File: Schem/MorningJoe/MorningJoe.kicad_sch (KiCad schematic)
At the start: 0 parts

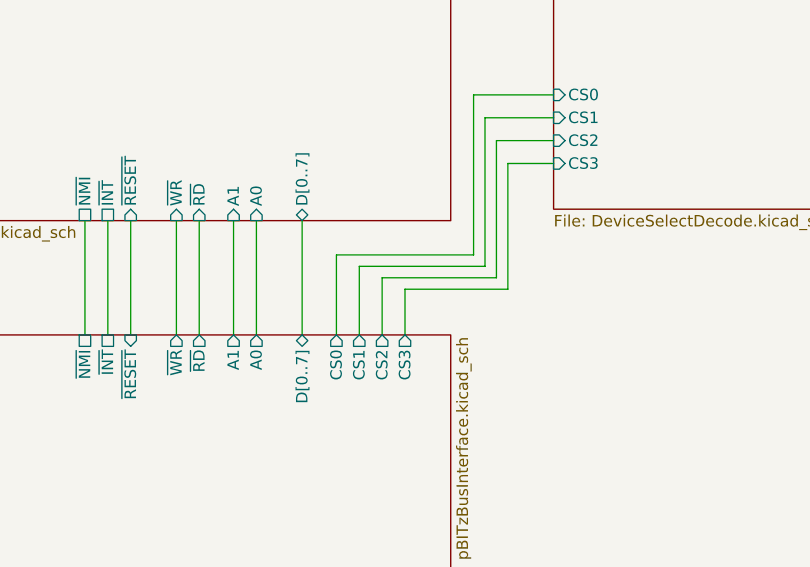
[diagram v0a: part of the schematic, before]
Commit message: Added both the Morning Joe and the Lunch Crema schematics, PCB, and KiCad library files.
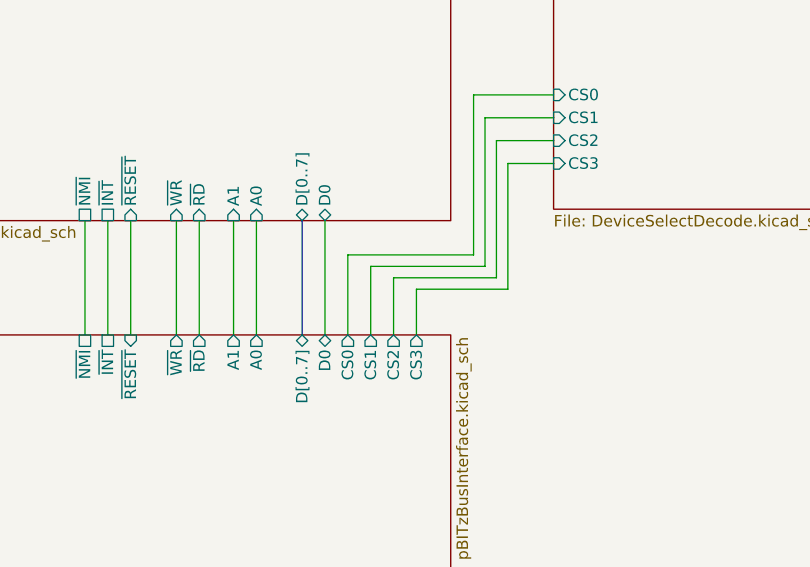
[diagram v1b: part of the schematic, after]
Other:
- sheet Video ports: added D0; removed none
- sheet pBITzInterface ports: added D0; removed none
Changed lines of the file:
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@@
 	(wire
+		(pts
+			(xy 104.14 88.9) (xy 109.22 88.9)
+		)
+		(stroke
+			(width 0)
+			(type default)
+		)
+	)
+	(wire
+		(pts
+			(xy 73.66 95.25) (xy 73.66 107.95)
+		)
+		(stroke
+			(width 0)
+			(type default)
+		)
+	)
+	(wire
+		(pts
+			(xy 93.98 102.87) (xy 104.14 102.87)
+		)
+		(stroke
+			(width 0)
+			(type default)
+		)
+	)
+	(wire
+		(pts
+			(xy 88.9 107.95) (xy 88.9 100.33)
+		)
+		(stroke
+			(width 0)
+			(type default)
+		)
+	)
+	(wire
+		(pts
+			(xy 59.69 95.25) (xy 59.69 107.95)
+		)
+		(stroke
+			(width 0)
+			(type default)
+		)
+	)
+	(wire
+		(pts
+			(xy 100.33 81.28) (xy 109.22 81.28)
+		)
+		(stroke
+			(width 0)
+			(type default)
+		)
+	)
+	(wire
+		(pts
+			(xy 91.44 101.6) (xy 102.87 101.6)
+		)
+		(stroke
+			(width 0)
+			(type default)
+		)
+	)
+	(wire
+		(pts
+			(xy 101.6 100.33) (xy 101.6 83.82)
+		)
+		(stroke
+			(width 0)
+			(type default)
+		)
+	)
+	(wire
+		(pts
+			(xy 69.85 95.25) (xy 69.85 107.95)
+		)
+		(stroke
+			(width 0)
+			(type default)
+		)
+	)
+	(wire
+		(pts
+			(xy 101.6 83.82) (xy 109.22 83.82)
+		)
+		(stroke
+			(width 0)
+			(type default)
+		)
+	)
+	(wire
+		(pts
+			(xy 102.87 86.36) (xy 109.22 86.36)
+		)
+		(stroke
+			(width 0)
+			(type default)
+		)
+	)
+	(wire
+		(pts
+			(xy 104.14 102.87) (xy 104.14 88.9)
+		)
+		(stroke
+			(width 0)
+			(type default)
+		)
+	)
+	(wire
+		(pts
+			(xy 57.15 95.25) (xy 57.15 107.95)
+		)
+		(stroke
+			(width 0)
+			(type default)
+		)
+	)
+	(bus
 		(pts
 			(xy 81.28 95.25) (xy 81.28 107.95)
@@
 	(wire
 		(pts
-			(xy 104.14 88.9) (xy 109.22 88.9)
-		)
-		(stroke
-			(width 0)
-			(type default)
-		)
-	)
-	(wire
-		(pts
-			(xy 73.66 95.25) (xy 73.66 107.95)
-		)
-		(stroke
-			(width 0)
-			(type default)
-		)
-	)
-	(wire
-		(pts
-			(xy 92.71 102.87) (xy 104.14 102.87)
-		)
-		(stroke
-			(width 0)
-			(type default)
-		)
-	)
-	(wire
-		(pts
-			(xy 87.63 107.95) (xy 87.63 100.33)
-		)
-		(stroke
-			(width 0)
-			(type default)
-		)
-	)
-	(wire
-		(pts
-			(xy 59.69 95.25) (xy 59.69 107.95)
-		)
-		(stroke
-			(width 0)
-			(type default)
-		)
-	)
-	(wire
-		(pts
-			(xy 100.33 81.28) (xy 109.22 81.28)
-		)
-		(stroke
-			(width 0)
-			(type default)
-		)
-	)
-	(wire
-		(pts
-			(xy 90.17 101.6) (xy 102.87 101.6)
-		)
-		(stroke
-			(width 0)
-			(type default)
-		)
-	)
-	(wire
-		(pts
-			(xy 101.6 100.33) (xy 101.6 83.82)
-		)
-		(stroke
-			(width 0)
-			(type default)
-		)
-	)
-	(wire
-		(pts
-			(xy 69.85 95.25) (xy 69.85 107.95)
-		)
-		(stroke
-			(width 0)
-			(type default)
-		)
-	)
-	(wire
-		(pts
-			(xy 101.6 83.82) (xy 109.22 83.82)
-		)
-		(stroke
-			(width 0)
-			(type default)
-		)
-	)
-	(wire
-		(pts
-			(xy 102.87 86.36) (xy 109.22 86.36)
-		)
-		(stroke
-			(width 0)
-			(type default)
-		)
-	)
-	(wire
-		(pts
-			(xy 104.14 102.87) (xy 104.14 88.9)
-		)
-		(stroke
-			(width 0)
-			(type default)
-		)
-	)
-	(wire
-		(pts
-			(xy 57.15 95.25) (xy 57.15 107.95)
-		)
-		(stroke
-			(width 0)
-			(type default)
-		)
-	)
-	(wire
-		(pts
 			(xy 67.31 95.25) (xy 67.31 107.95)
 		)
@@
 	(wire
 		(pts
-			(xy 87.63 100.33) (xy 101.6 100.33)
-		)
-		(stroke
-			(width 0)
-			(type default)
-		)
-	)
-	(wire
-		(pts
-			(xy 90.17 107.95) (xy 90.17 101.6)
+			(xy 88.9 100.33) (xy 101.6 100.33)
+		)
+		(stroke
+			(width 0)
+			(type default)
+		)
+	)
+	(wire
+		(pts
+			(xy 91.44 107.95) (xy 91.44 101.6)
 		)
 		(stroke
@@
 	(wire
 		(pts
-			(xy 85.09 99.06) (xy 100.33 99.06)
+			(xy 86.36 99.06) (xy 100.33 99.06)
 		)
 		(stroke
@@
 	(wire
 		(pts
-			(xy 85.09 107.95) (xy 85.09 99.06)
-		)
-		(stroke
-			(width 0)
-			(type default)
-		)
-	)
-	(wire
-		(pts
-			(xy 92.71 107.95) (xy 92.71 102.87)
+			(xy 83.82 95.25) (xy 83.82 107.95)
+		)
+		(stroke
+			(width 0)
+			(type default)
+		)
+	)
+	(wire
+		(pts
+			(xy 86.36 107.95) (xy 86.36 99.06)
+		)
+		(stroke
+			(width 0)
+			(type default)
+		)
+	)
+	(wire
+		(pts
+			(xy 93.98 107.95) (xy 93.98 102.87)
 		)
 		(stroke
@@
 			)
 		)
+		(pin "D0" bidirectional
+			(at 83.82 95.25 270)
+			(effects
+				(font
+					(size 1.27 1.27)
+				)
+				(justify left)
+			)
+		)
 		(instances
 			(project "MorningJoe"
@@
 		)
 		(pin "CS0" output
-			(at 85.09 107.95 90)
+			(at 86.36 107.95 90)
 			(effects
 				(font
@@
 		)
 		(pin "CS1" output
-			(at 87.63 107.95 90)
+			(at 88.9 107.95 90)
 			(effects
 				(font
@@
 		)
 		(pin "CS3" output
-			(at 92.71 107.95 90)
+			(at 93.98 107.95 90)
 			(effects
 				(font
@@
 		)
 		(pin "CS2" output
-			(at 90.17 107.95 90)
+			(at 91.44 107.95 90)
 			(effects
 				(font
@@
 			(effects
 				(font
+					(size 1.27 1.27)
+				)
+				(justify right)
+			)
+		)
+		(pin "D0" bidirectional
+			(at 83.82 107.95 90)
+			(effects
+				(font
